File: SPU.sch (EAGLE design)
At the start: 414 parts, among them Q1 BSS123, Q2 12MHz, Q3 BSS123, Q4 BSS123, Q5 BSS123, Q6 BSS123

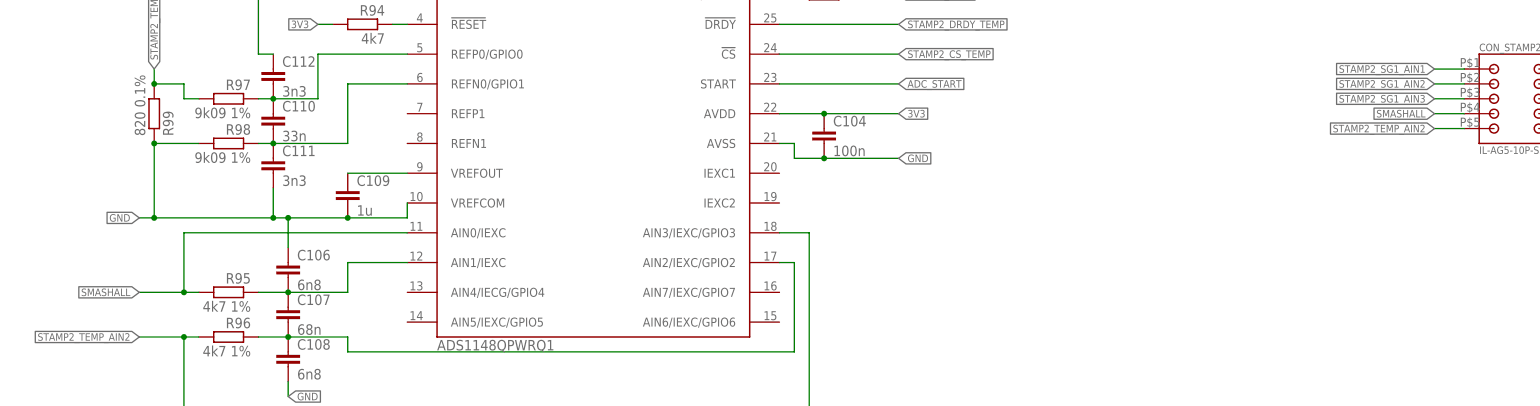
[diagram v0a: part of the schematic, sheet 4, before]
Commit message: End of day commit Schematic: Removed renaming error Bord: Placed and routed Stamp 2
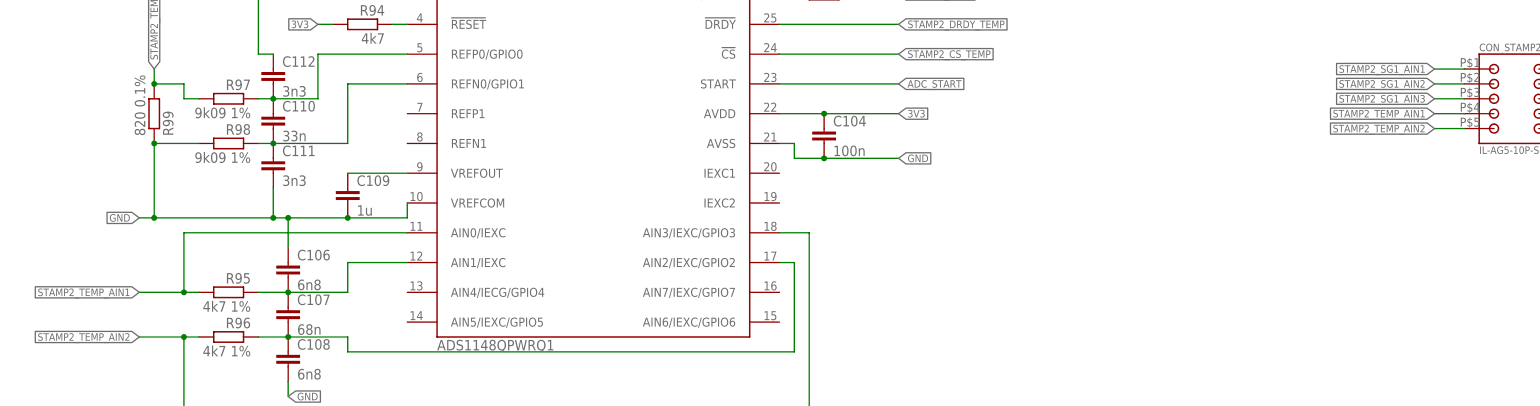
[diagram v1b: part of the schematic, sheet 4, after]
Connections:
- net N$110 renamed S2AT2
- net N$111 renamed S2AT1
- net SMASHALL renamed STAMP2_TEMP_AIN1
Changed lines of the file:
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@@
 </segment>
 </net>
-<net name="SMASHALL" class="0">
-<segment>
-<pinref part="R95" gate="G$1" pin="2"/>
-<wire x1="45.72" y1="45.72" x2="43.18" y2="45.72" width="0.1524" layer="91"/>
-<pinref part="STAMP2_ADC_TEMP" gate="G$1" pin="AIN0/IEXC"/>
-<wire x1="43.18" y1="45.72" x2="35.56" y2="45.72" width="0.1524" layer="91"/>
-<wire x1="81.28" y1="55.88" x2="43.18" y2="55.88" width="0.1524" layer="91"/>
-<wire x1="43.18" y1="55.88" x2="43.18" y2="45.72" width="0.1524" layer="91"/>
-<junction x="43.18" y="45.72"/>
-<label x="35.56" y="45.72" size="1.27" layer="95" rot="R180" xref="yes"/>
-</segment>
-<segment>
-<pinref part="CON_STAMP2" gate="G$1" pin="P$4"/>
-<wire x1="261.62" y1="76.2" x2="256.54" y2="76.2" width="0.1524" layer="91"/>
-<label x="256.54" y="76.2" size="1.27" layer="95" rot="R180" xref="yes"/>
-</segment>
-</net>
-<net name="N$110" class="0">
+<net name="S2AT2" class="0">
 <segment>
 <pinref part="C110" gate="G$1" pin="2"/>
@@
 </segment>
 </net>
-<net name="N$111" class="0">
+<net name="S2AT1" class="0">
 <segment>
 <pinref part="C110" gate="G$1" pin="1"/>
@@
 </segment>
 </net>
+<net name="STAMP2_TEMP_AIN1" class="0">
+<segment>
+<pinref part="R95" gate="G$1" pin="2"/>
+<wire x1="45.72" y1="45.72" x2="43.18" y2="45.72" width="0.1524" layer="91"/>
+<pinref part="STAMP2_ADC_TEMP" gate="G$1" pin="AIN0/IEXC"/>
+<wire x1="43.18" y1="45.72" x2="35.56" y2="45.72" width="0.1524" layer="91"/>
+<wire x1="81.28" y1="55.88" x2="43.18" y2="55.88" width="0.1524" layer="91"/>
+<wire x1="43.18" y1="55.88" x2="43.18" y2="45.72" width="0.1524" layer="91"/>
+<junction x="43.18" y="45.72"/>
+<label x="35.56" y="45.72" size="1.27" layer="95" rot="R180" xref="yes"/>
+</segment>
+<segment>
+<pinref part="CON_STAMP2" gate="G$1" pin="P$4"/>
+<wire x1="261.62" y1="76.2" x2="256.54" y2="76.2" width="0.1524" layer="91"/>
+<label x="256.54" y="76.2" size="1.27" layer="95" rot="R180" xref="yes"/>
+</segment>
+</net>

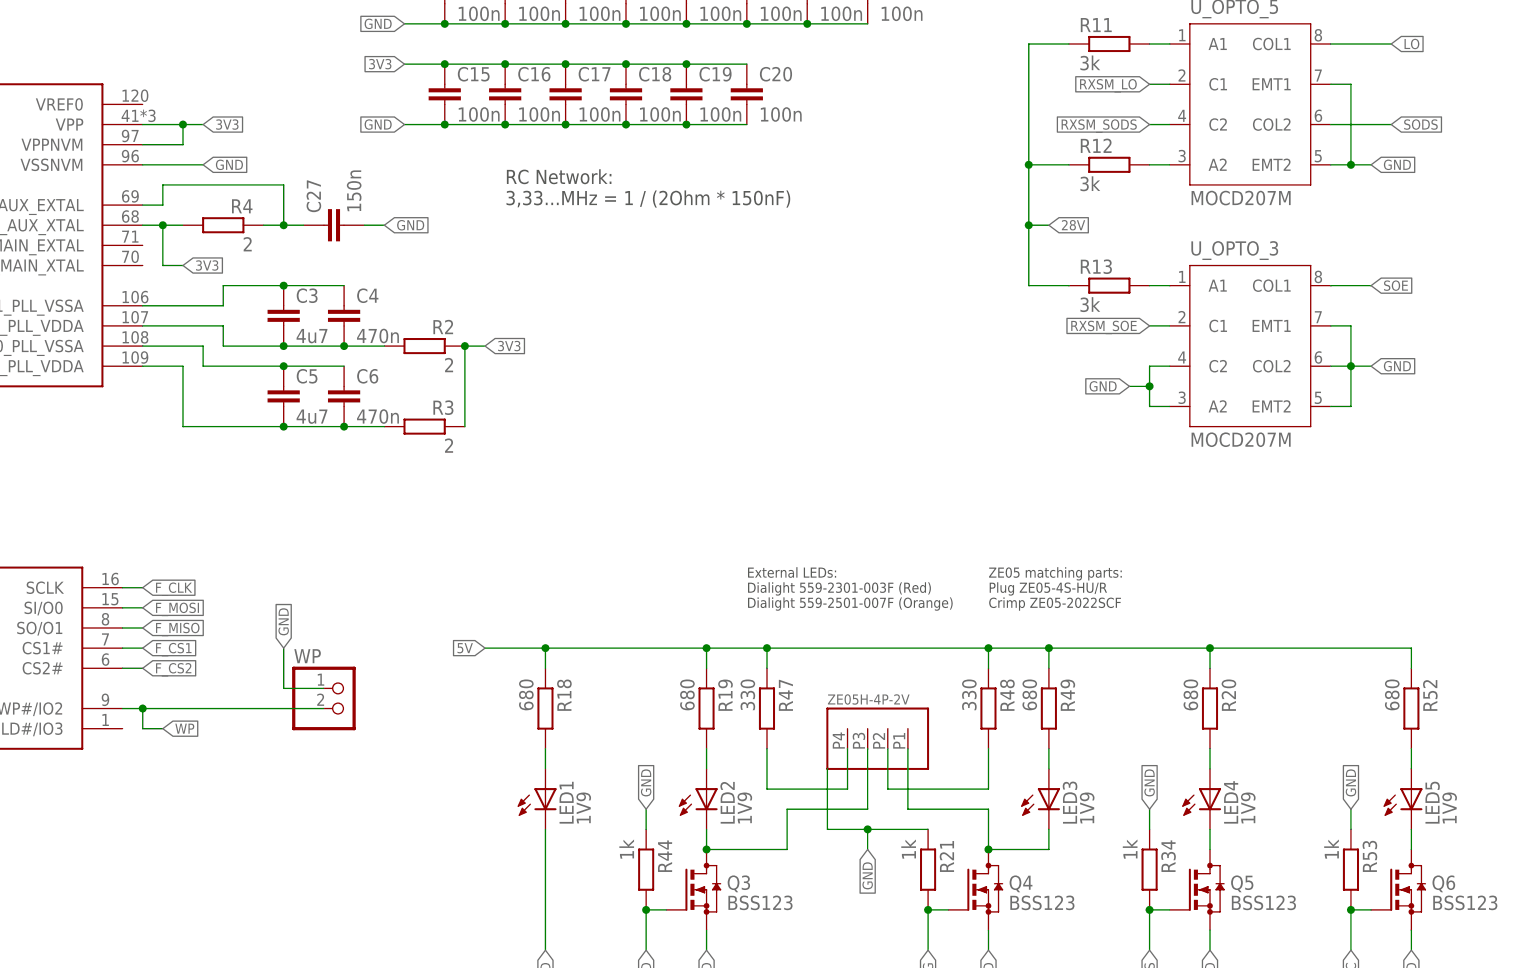
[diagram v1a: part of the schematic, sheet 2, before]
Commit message: Routed all signals and voltages End of day commit TODO: GND connection Adding WE - XTAL Eagle lib Update schematic: Adding XTAL Bord: routed
NOTE: DRC not ok
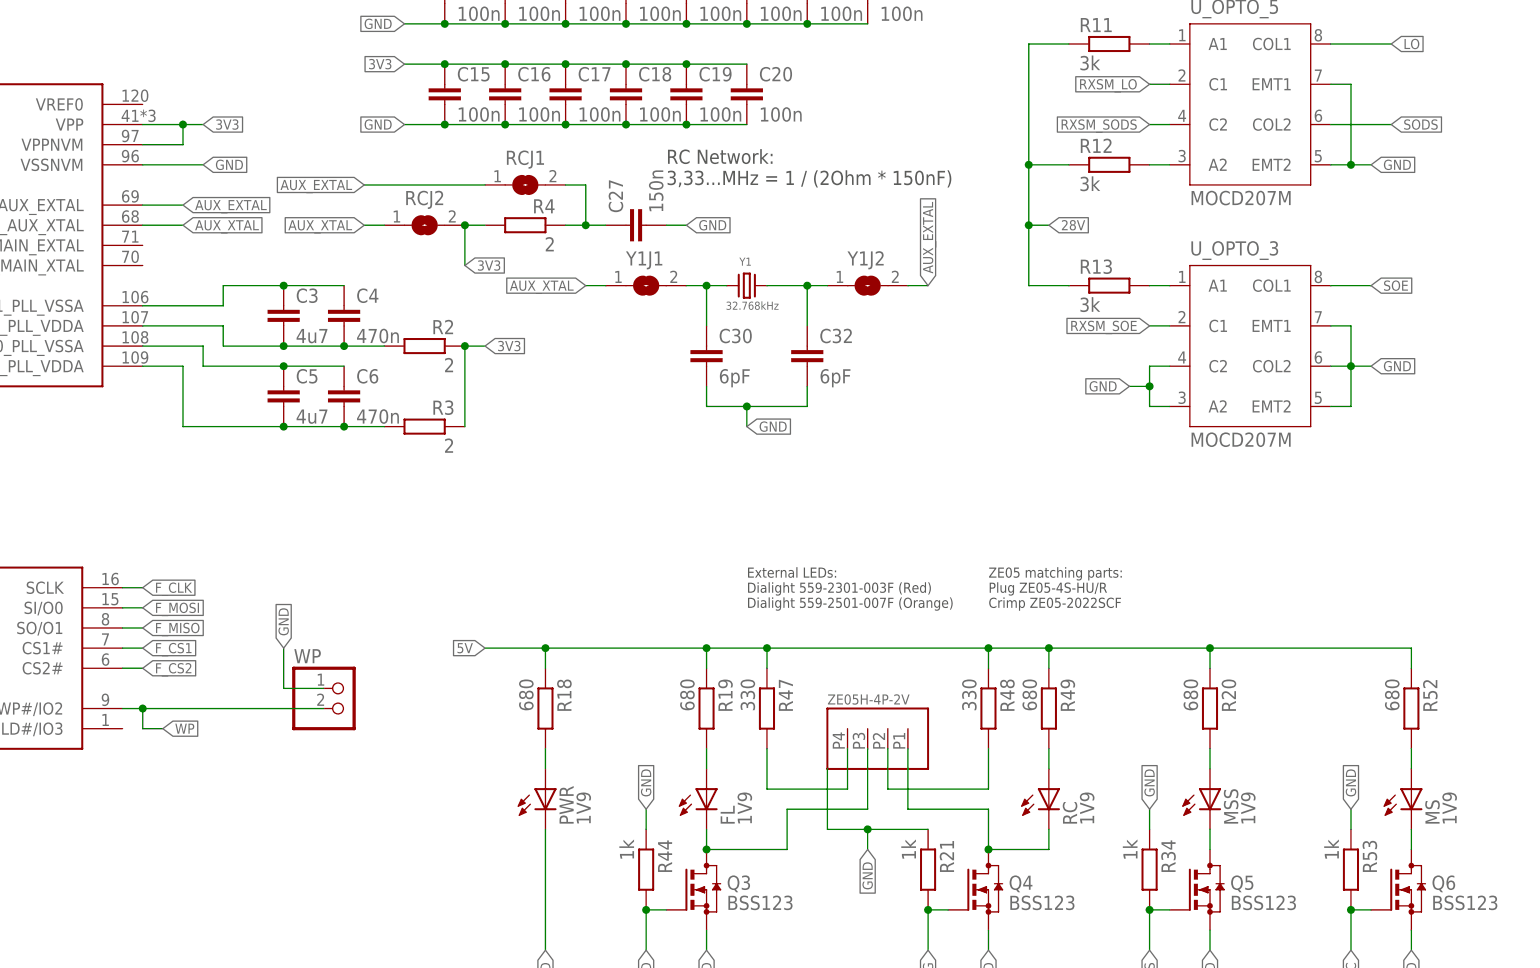
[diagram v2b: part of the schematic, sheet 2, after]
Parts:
- added C30, C32: 6pF, rcl:C-EUC0805
- added RCJ1, RCJ2, Y1J1, Y1J2: (no value), jumper:SJ
- added Y1: 32.768kHz, Eagle_WE-XTAL (rev21c):WE-XTAL_IQXC-90_830107088501
- renumbered LED1 to PWR, LED2 to FL, LED3 to RC, LED4 to MSS, LED5 to MS
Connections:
- removed net N$33: C27.1, R4.1, SF2_M2S010TQ1G$7.XTLOSC_AUX_EXTAL
- new net AUX_EXTAL: RCJ1.1, SF2_M2S010TQ1G$7.XTLOSC_AUX_EXTAL, Y1J2.2
- new net AUX_XTAL: RCJ2.1, SF2_M2S010TQ1G$7.XTLOSC_AUX_XTAL, Y1J1.1
- new net N$76: C32.1, Y1.2, Y1J2.1
- new net N$8: C30.1, Y1.1, Y1J1.2
- new net NET_U: C27.1, R4.1, RCJ1.2
- net 3V3: now also RCJ2.2; no longer SF2_M2S010TQ1G$7.XTLOSC_AUX_XTAL
- net GND: now also C30.2, C32.2
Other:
- moved on the sheet: C27, R4

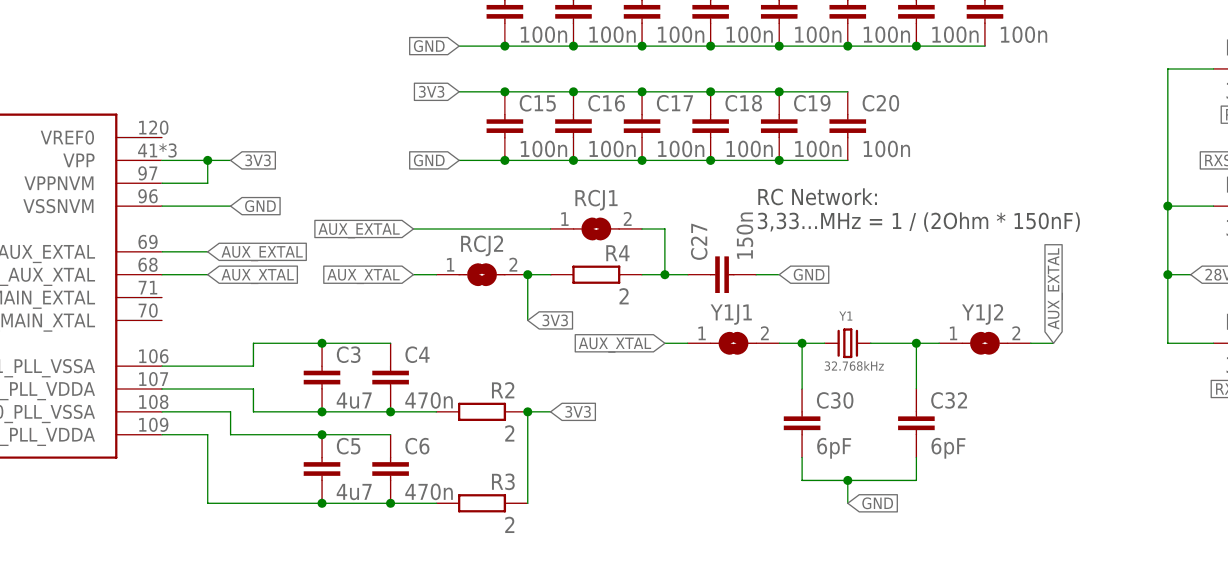
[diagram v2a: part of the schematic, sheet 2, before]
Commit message: Minor changes
- XTAL from AUX to MAIN
- Removes authors
- Adds interface measurements
- Fixes Airwire / Wirestub
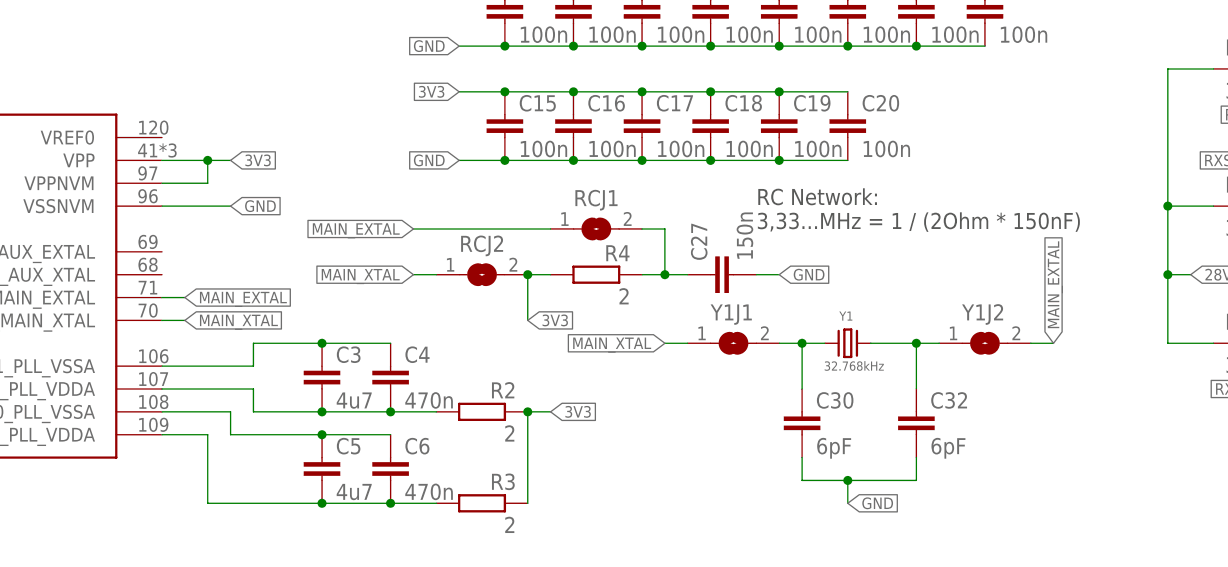
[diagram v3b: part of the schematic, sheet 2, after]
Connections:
- removed net AUX_EXTAL: RCJ1.1, SF2_M2S010TQ1G$7.XTLOSC_AUX_EXTAL, Y1J2.2
- removed net AUX_XTAL: RCJ2.1, SF2_M2S010TQ1G$7.XTLOSC_AUX_XTAL, Y1J1.1
- new net MAIN_EXTAL: RCJ1.1, SF2_M2S010TQ1G$7.XTLOSC_MAIN_EXTAL, Y1J2.2
- new net MAIN_XTAL: RCJ2.1, SF2_M2S010TQ1G$7.XTLOSC_MAIN_XTAL, Y1J1.1
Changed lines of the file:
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@@
 </segment>
 </net>
-<net name="AUX_EXTAL" class="0">
-<segment>
-<pinref part="SF2_M2S010TQ1" gate="G$7" pin="XTLOSC_AUX_EXTAL"/>
-<wire x1="200.66" y1="152.4" x2="205.74" y2="152.4" width="0.1524" layer="91"/>
-<label x="205.74" y="152.4" size="1.27" layer="95" xref="yes"/>
-</segment>
+<net name="MAIN_EXTAL" class="0">
 <segment>
 <wire x1="243.84" y1="154.94" x2="228.6" y2="154.94" width="0.1524" layer="91"/>
@@
 <pinref part="Y1J2" gate="1" pin="2"/>
 </segment>
+<segment>
+<pinref part="SF2_M2S010TQ1" gate="G$7" pin="XTLOSC_MAIN_EXTAL"/>
+<wire x1="200.66" y1="147.32" x2="203.2" y2="147.32" width="0.1524" layer="91"/>
+<label x="203.2" y="147.32" size="1.27" layer="95" xref="yes"/>
+</segment>
 </net>
-<net name="AUX_XTAL" class="0">
-<segment>
-<pinref part="SF2_M2S010TQ1" gate="G$7" pin="XTLOSC_AUX_XTAL"/>
-<wire x1="200.66" y1="149.86" x2="205.74" y2="149.86" width="0.1524" layer="91"/>
-<label x="205.74" y="149.86" size="1.27" layer="95" xref="yes"/>
-</segment>
+<net name="MAIN_XTAL" class="0">
 <segment>
 <wire x1="231.14" y1="149.86" x2="228.6" y2="149.86" width="0.1524" layer="91"/>
@@
 <pinref part="Y1J1" gate="1" pin="1"/>
 </segment>
+<segment>
+<pinref part="SF2_M2S010TQ1" gate="G$7" pin="XTLOSC_MAIN_XTAL"/>
+<wire x1="200.66" y1="144.78" x2="203.2" y2="144.78" width="0.1524" layer="91"/>
+<label x="203.2" y="144.78" size="1.27" layer="95" xref="yes"/>
+</segment>
 </net>
